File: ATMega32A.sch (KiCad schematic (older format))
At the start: 21 parts, among them J201 AVR-ISP-6, J202 UART, U201 ATmega32A-AU, Y201 16MHz

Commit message: Updating Atmega32A subboard
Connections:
- net labels added: A0, A1, A2, A3, A4, A5, A6, A7
- wire segments 56 -> 63

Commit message: Placing hierarchical labels on ATMega32A
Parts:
- added C?: 100n, Capacitor_SMD:C_0805_2012Metric_Pad1.15x1.40mm_HandSolder, symbol Device:C
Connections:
- net labels added: D1, D10_INT0, D11_INT1, D12_PWM, D13PWM, D14_PWM, D15_PWM, D16_SCL, D17_SDA, D18, D19, D2, D20, D21, D22, D23, D3, D4, D5, D6, D7, D8_Rx, D9_Tx, RST
- net labels removed: +12V, 1, 10_INT0, 11_INT1, 12_PWM, 13_PWM, 14_PWM, 15_PWM, 16_SCL, 17_SDA, 18, 19, 20, 21, 22, 23, 24_A0, 25_A1, 26_A2, 27_A3, 28_A4, 29_A5, 2_INT2, 30_A6, 31_A7, 3_PWM, 4_PWM
- wire segments 63 -> 93
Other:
- moved on the sheet: C?, R?

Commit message: Subboard done
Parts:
- removed C205, C207: 100n, Capacitor_SMD:C_1206_3216Metric_Pad1.42x1.75mm_HandSolder, symbol Device:C
- removed C206, C208: 100n, Capacitor_SMD:C_0805_2012Metric_Pad1.15x1.40mm_HandSolder, symbol Device:C
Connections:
- net D5 is gone; now on net 5_MOSI: U201.1 (PB5)
- net D6 is gone; now on net 6_MISO: U201.2 (PB6)
- net D7 is gone; now on net 7_SCK: U201.3 (PB7)
- net D13PWM renamed D13_PWM
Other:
- moved on the sheet: C?, R?

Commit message: Front LED
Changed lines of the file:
@@
 Text HLabel 2050 1150 0    97   Input ~ 0
 GND32
+Text HLabel 3000 1150 2    97   Input ~ 0
+GNDA32
 $EndSCHEMATC

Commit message: Cleanup MasterSCH
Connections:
- net D2 renamed D2_INT2
- net D3 renamed D3_OC0
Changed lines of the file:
@@
 D1
 Text HLabel 7000 3100 2    97   Input ~ 0
-D2
+D2_INT2
 Text HLabel 7000 3200 2    97   Input ~ 0
-D3
+D3_OC0
 Text HLabel 7000 3300 2    97   Input ~ 0
 D4

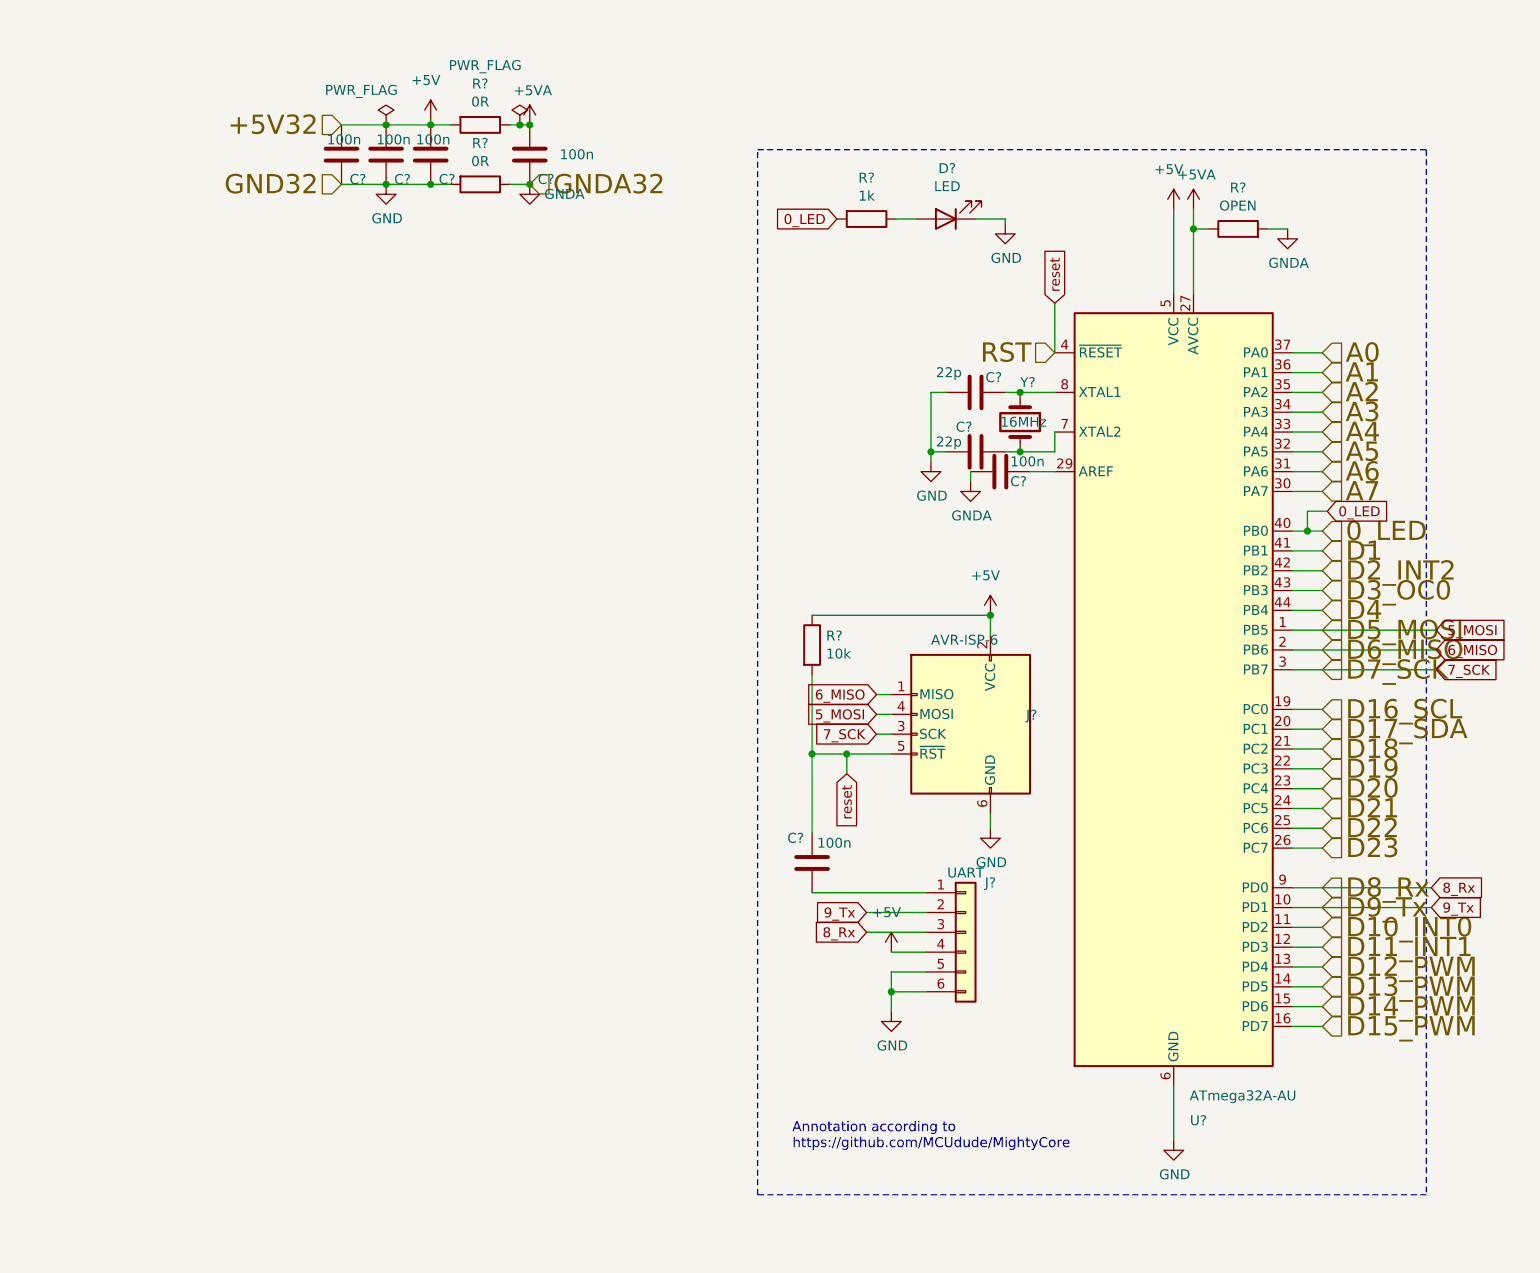
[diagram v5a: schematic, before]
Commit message: 5VA on Atmega32A
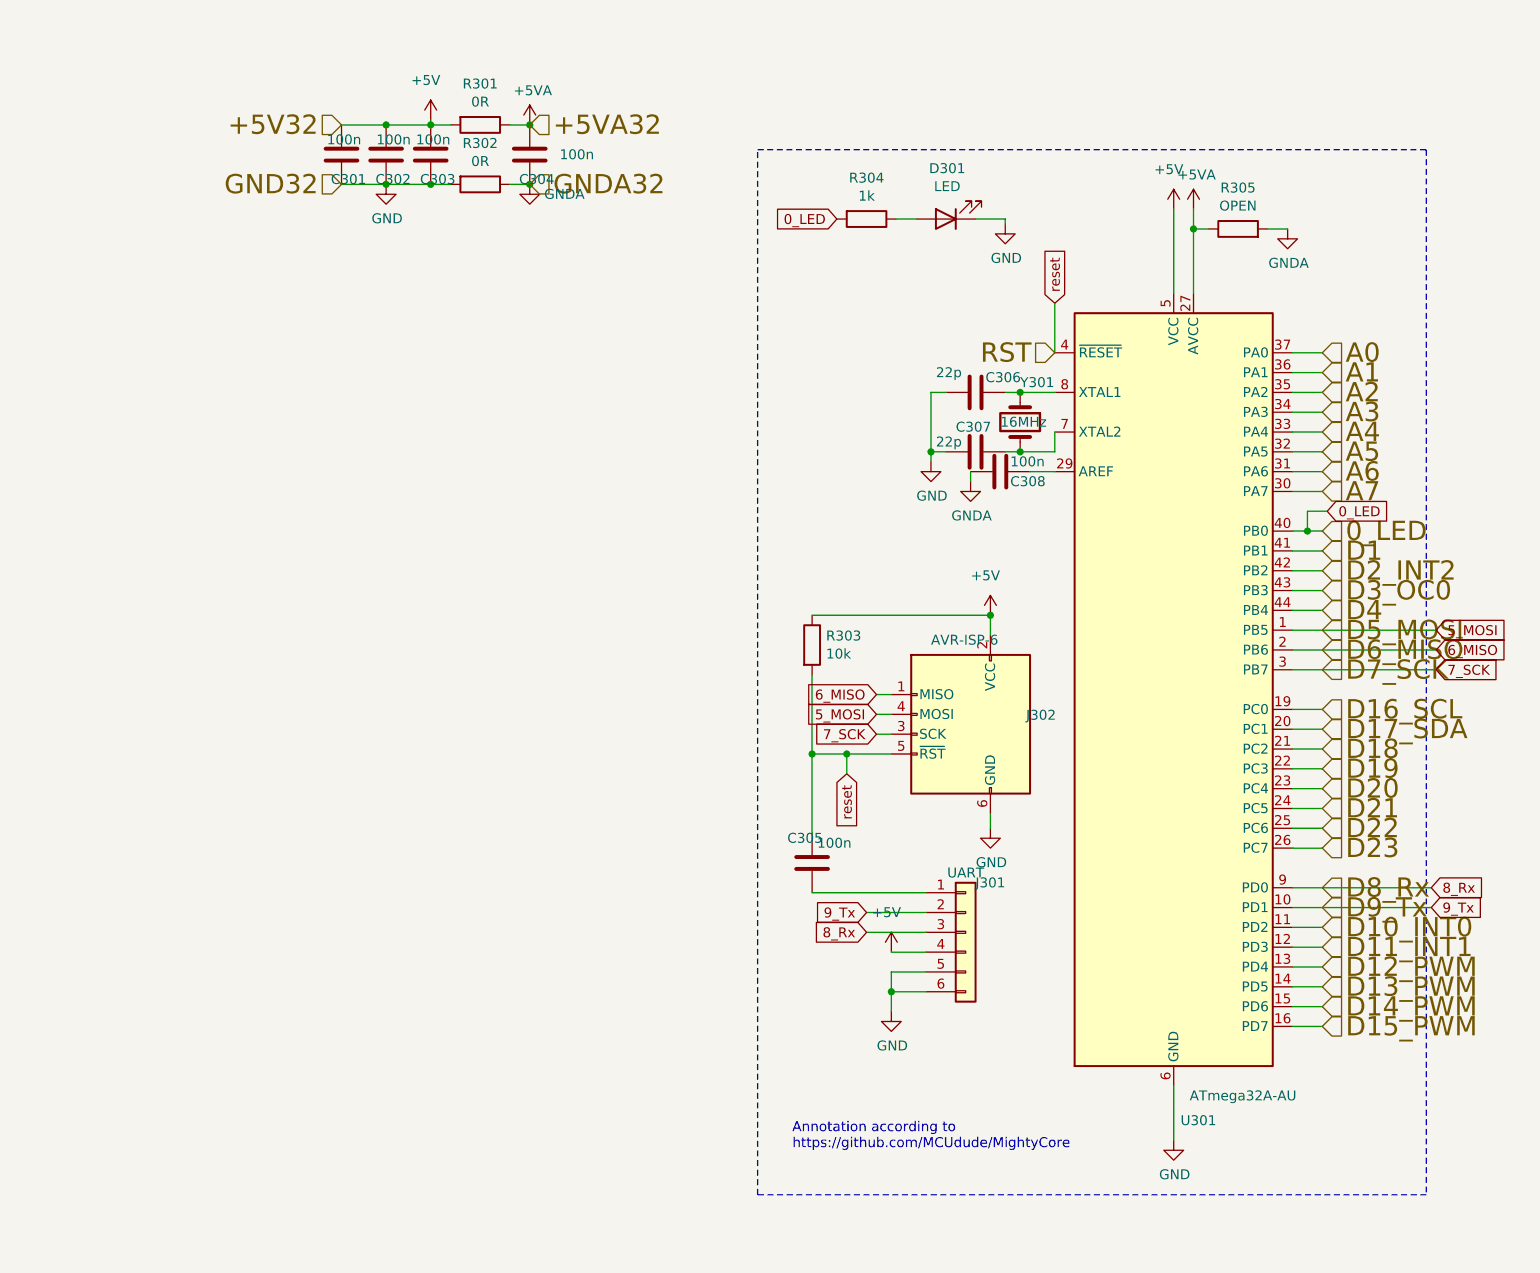
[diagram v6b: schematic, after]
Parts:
- gave numbers to parts that had none: 1

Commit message: Initial footprints and netlist
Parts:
- C201, C202, C203, C204, C209, C210, C211, C308: footprint Capacitor_SMD:C_0805_2012Metric_Pad1.15x1.40mm_HandSolder -> AJ:C_0805_AJ
- D201: footprint LED_SMD:LED_0805_2012Metric_Pad1.15x1.40mm_HandSolder -> AJ:D_0805_AJ
- R201, R202, R203, R205: footprint Resistor_SMD:R_0805_2012Metric_Pad1.15x1.40mm_HandSolder -> AJ:R_0805_AJ
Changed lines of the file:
@@
 F 0 "C305" H 4300 4700 50  0000 L CNN
 F 1 "100n" H 4450 4675 50  0000 L CNN
-F 2 "Capacitor_SMD:C_0805_2012Metric_Pad1.15x1.40mm_HandSolder" H 4463 4425 50  0001 C CNN
+F 2 "AJ:C_0805_AJ" H 4463 4425 50  0001 C CNN
 F 3 "~" H 4425 4575 50  0001 C CNN
 	1    4425 4575
@@
 F 0 "R303" H 4495 3521 50  0000 L CNN
 F 1 "10k" H 4495 3430 50  0000 L CNN
-F 2 "Resistor_SMD:R_0805_2012Metric_Pad1.15x1.40mm_HandSolder" V 4355 3475 50  0001 C CNN
+F 2 "AJ:R_0805_AJ" V 4355 3475 50  0001 C CNN
 F 3 "~" H 4425 3475 50  0001 C CNN
 	1    4425 3475
@@
 F 0 "C307" V 5125 2400 50  0000 L CNN
 F 1 "22p" V 5200 2300 50  0000 L CNN
-F 2 "Capacitor_SMD:C_0805_2012Metric_Pad1.15x1.40mm_HandSolder" H 5288 2350 50  0001 C CNN
+F 2 "AJ:C_0805_AJ" H 5288 2350 50  0001 C CNN
 F 3 "~" H 5250 2500 50  0001 C CNN
 	1    5250 2500
@@
 F 0 "C306" V 5175 2250 50  0000 L CNN
 F 1 "22p" V 5150 2000 50  0000 L CNN
-F 2 "Capacitor_SMD:C_0805_2012Metric_Pad1.15x1.40mm_HandSolder" H 5288 2050 50  0001 C CNN
+F 2 "AJ:C_0805_AJ" H 5288 2050 50  0001 C CNN
 F 3 "~" H 5250 2200 50  0001 C CNN
 	1    5250 2200
@@
 F 0 "R304" V 4493 1325 50  0000 C CNN
 F 1 "1k" V 4584 1325 50  0000 C CNN
-F 2 "Resistor_SMD:R_0805_2012Metric_Pad1.15x1.40mm_HandSolder" V 4630 1325 50  0001 C CNN
+F 2 "AJ:R_0805_AJ" V 4630 1325 50  0001 C CNN
 F 3 "~" H 4700 1325 50  0001 C CNN
 	1    4700 1325
@@
 F 0 "D301" H 5093 1070 50  0000 C CNN
 F 1 "LED" H 5093 1161 50  0000 C CNN
-F 2 "LED_SMD:LED_0805_2012Metric_Pad1.15x1.40mm_HandSolder" H 5100 1325 50  0001 C CNN
+F 2 "AJ:D_0805_AJ" H 5100 1325 50  0001 C CNN
 F 3 "~" H 5100 1325 50  0001 C CNN
 	1    5100 1325
@@
 F 0 "R305" V 6782 1375 50  0000 C CNN
 F 1 "OPEN" V 6691 1375 50  0000 C CNN
-F 2 "Resistor_SMD:R_0805_2012Metric_Pad1.15x1.40mm_HandSolder" V 6505 1375 50  0001 C CNN
+F 2 "AJ:R_0805_AJ" V 6505 1375 50  0001 C CNN
 F 3 "~" H 6575 1375 50  0001 C CNN
 	1    6575 1375
@@
 F 0 "R301" V 2543 850 50  0000 C CNN
 F 1 "0R" V 2634 850 50  0000 C CNN
-F 2 "Resistor_SMD:R_0805_2012Metric_Pad1.15x1.40mm_HandSolder" V 2680 850 50  0001 C CNN
+F 2 "AJ:R_0805_AJ" V 2680 850 50  0001 C CNN
 F 3 "~" H 2750 850 50  0001 C CNN
 	1    2750 850
@@
 F 0 "C304" H 2875 1125 50  0000 L CNN
 F 1 "100n" H 2675 1000 50  0000 L CNN
-F 2 "Capacitor_SMD:C_0805_2012Metric_Pad1.15x1.40mm_HandSolder" H 3038 850 50  0001 C CNN
+F 2 "AJ:C_0805_AJ" H 3038 850 50  0001 C CNN
 F 3 "~" H 3000 1000 50  0001 C CNN
 	1    3000 1000
@@
 F 0 "C303" H 2375 1125 50  0000 L CNN
 F 1 "100n" H 2400 925 50  0000 L CNN
-F 2 "Capacitor_SMD:C_0805_2012Metric_Pad1.15x1.40mm_HandSolder" H 2538 850 50  0001 C CNN
+F 2 "AJ:C_0805_AJ" H 2538 850 50  0001 C CNN
 F 3 "~" H 2500 1000 50  0001 C CNN
 	1    2500 1000
@@
 F 0 "C302" H 2150 1125 50  0000 L CNN
 F 1 "100n" H 2150 925 50  0000 L CNN
-F 2 "Capacitor_SMD:C_0805_2012Metric_Pad1.15x1.40mm_HandSolder" H 2313 850 50  0001 C CNN
+F 2 "AJ:C_0805_AJ" H 2313 850 50  0001 C CNN
 F 3 "~" H 2275 1000 50  0001 C CNN
 	1    2275 1000
@@
 F 0 "C301" H 1925 1125 50  0000 L CNN
 F 1 "100n" H 1950 925 50  0000 L CNN
-F 2 "Capacitor_SMD:C_0805_2012Metric_Pad1.15x1.40mm_HandSolder" H 2088 850 50  0001 C CNN
+F 2 "AJ:C_0805_AJ" H 2088 850 50  0001 C CNN
 F 3 "~" H 2050 1000 50  0001 C CNN
 	1    2050 1000
@@
 Wire Wire Line
 	6850 2900 6925 2900
-Wire Wire Line
-	6850 3000 7000 3000
-Wire Wire Line
-	7000 3100 6850 3100
-Wire Wire Line
-	6850 3200 7000 3200
-Wire Wire Line
-	7000 3300 6850 3300
 Wire Wire Line
 	6850 2700 7000 2700
@@
 F 0 "C308" V 5425 2650 50  0000 L CNN
 F 1 "100n" V 5325 2650 50  0000 L CNN
-F 2 "Capacitor_SMD:C_0805_2012Metric_Pad1.15x1.40mm_HandSolder" H 5413 2450 50  0001 C CNN
+F 2 "AJ:C_0805_AJ" H 5413 2450 50  0001 C CNN
 F 3 "~" H 5375 2600 50  0001 C CNN
 	1    5375 2600
@@
 Wire Wire Line
 	2900 850  3000 850
+Wire Wire Line
+	6850 3000 7000 3000
+Wire Wire Line
+	6850 3100 7000 3100
+Wire Wire Line
+	7000 3200 6850 3200
+Wire Wire Line
+	6850 3300 7000 3300
 $EndSCHEMATC

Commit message: Encoder 2
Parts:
- renumbered C201 to C301, C202 to C302, C203 to C303, C204 to C304, C211 to C305, C209 to C306, C210 to C307, D201 to D301, J202 to J301, J201 to J302, R201 to R301, R204 to R302, R205 to R303, R202 to R304, R203 to R305, U201 to U301, Y201 to Y301
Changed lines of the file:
@@
 P 6250 3700
 AR Path="/5CD50179" Ref="U?"  Part="1"
-AR Path="/5CD3F059/5CD50179" Ref="U201"  Part="1"
+AR Path="/5CD3F059/5CD50179" Ref="U?"  Part="1"
 AR Path="/608CA457/5CD3F059/5CD50179" Ref="U301"  Part="1"
 F 0 "U301" H 6375 1525 50  0000 C CNN
@@
 P 5225 3925
 AR Path="/5CD5017F" Ref="J?"  Part="1"
-AR Path="/5CD3F059/5CD5017F" Ref="J201"  Part="1"
+AR Path="/5CD3F059/5CD5017F" Ref="J?"  Part="1"
 AR Path="/608CA457/5CD3F059/5CD5017F" Ref="J302"  Part="1"
 F 0 "J302" H 4945 4021 50  0000 R CNN
@@
 P 5200 4925
 AR Path="/5CD50185" Ref="J?"  Part="1"
-AR Path="/5CD3F059/5CD50185" Ref="J202"  Part="1"
+AR Path="/5CD3F059/5CD50185" Ref="J?"  Part="1"
 AR Path="/608CA457/5CD3F059/5CD50185" Ref="J301"  Part="1"
 F 0 "J301" H 5325 5175 50  0000 C CNN
@@
 P 4425 4575
 AR Path="/5CD5019E" Ref="C?"  Part="1"
-AR Path="/5CD3F059/5CD5019E" Ref="C211"  Part="1"
+AR Path="/5CD3F059/5CD5019E" Ref="C?"  Part="1"
 AR Path="/608CA457/5CD3F059/5CD5019E" Ref="C305"  Part="1"
 F 0 "C305" H 4300 4700 50  0000 L CNN
@@
 P 4425 3475
 AR Path="/5CD501A6" Ref="R?"  Part="1"
-AR Path="/5CD3F059/5CD501A6" Ref="R205"  Part="1"
+AR Path="/5CD3F059/5CD501A6" Ref="R?"  Part="1"
 AR Path="/608CA457/5CD3F059/5CD501A6" Ref="R303"  Part="1"
 F 0 "R303" H 4495 3521 50  0000 L CNN
@@
 P 5475 2350
 AR Path="/5CD501CD" Ref="Y?"  Part="1"
-AR Path="/5CD3F059/5CD501CD" Ref="Y201"  Part="1"
+AR Path="/5CD3F059/5CD501CD" Ref="Y?"  Part="1"
 AR Path="/608CA457/5CD3F059/5CD501CD" Ref="Y301"  Part="1"
 F 0 "Y301" V 5275 2350 50  0000 L CNN
@@
 P 5250 2500
 AR Path="/5CD501D9" Ref="C?"  Part="1"
-AR Path="/5CD3F059/5CD501D9" Ref="C210"  Part="1"
+AR Path="/5CD3F059/5CD501D9" Ref="C?"  Part="1"
 AR Path="/608CA457/5CD3F059/5CD501D9" Ref="C307"  Part="1"
 F 0 "C307" V 5125 2400 50  0000 L CNN
@@
 P 5250 2200
 AR Path="/5CD501E0" Ref="C?"  Part="1"
-AR Path="/5CD3F059/5CD501E0" Ref="C209"  Part="1"
+AR Path="/5CD3F059/5CD501E0" Ref="C?"  Part="1"
 AR Path="/608CA457/5CD3F059/5CD501E0" Ref="C306"  Part="1"
 F 0 "C306" V 5175 2250 50  0000 L CNN
@@
 P 6825 1375
 AR Path="/5CD501E9" Ref="#PWR?"  Part="1"
-AR Path="/5CD3F059/5CD501E9" Ref="#PWR0206"  Part="1"
+AR Path="/5CD3F059/5CD501E9" Ref="#PWR?"  Part="1"
 AR Path="/608CA457/5CD3F059/5CD501E9" Ref="#PWR0315"  Part="1"
 F 0 "#PWR0315" H 6825 1125 50  0001 C CNN
@@
 P 5225 2650
 AR Path="/5CD501EF" Ref="#PWR?"  Part="1"
-AR Path="/5CD3F059/5CD501EF" Ref="#PWR0214"  Part="1"
+AR Path="/5CD3F059/5CD501EF" Ref="#PWR?"  Part="1"
 AR Path="/608CA457/5CD3F059/5CD501EF" Ref="#PWR0308"  Part="1"
 F 0 "#PWR0308" H 5225 2400 50  0001 C CNN
@@
 P 4700 1325
 AR Path="/5CD501F7" Ref="R?"  Part="1"
-AR Path="/5CD3F059/5CD501F7" Ref="R202"  Part="1"
+AR Path="/5CD3F059/5CD501F7" Ref="R?"  Part="1"
 AR Path="/608CA457/5CD3F059/5CD501F7" Ref="R304"  Part="1"
 F 0 "R304" V 4493 1325 50  0000 C CNN
@@
 P 5100 1325
 AR Path="/5CD501FD" Ref="D?"  Part="1"
-AR Path="/5CD3F059/5CD501FD" Ref="D201"  Part="1"
+AR Path="/5CD3F059/5CD501FD" Ref="D?"  Part="1"
 AR Path="/608CA457/5CD3F059/5CD501FD" Ref="D301"  Part="1"
 F 0 "D301" H 5093 1070 50  0000 C CNN
@@
 P 6575 1375
 AR Path="/5CD5023A" Ref="R?"  Part="1"
-AR Path="/5CD3F059/5CD5023A" Ref="R203"  Part="1"
+AR Path="/5CD3F059/5CD5023A" Ref="R?"  Part="1"
 AR Path="/608CA457/5CD3F059/5CD5023A" Ref="R305"  Part="1"
 F 0 "R305" V 6782 1375 50  0000 C CNN
@@
 P 6350 1275
 AR Path="/5CD5024D" Ref="#PWR?"  Part="1"
-AR Path="/5CD3F059/5CD5024D" Ref="#PWR0203"  Part="1"
+AR Path="/5CD3F059/5CD5024D" Ref="#PWR?"  Part="1"
 AR Path="/608CA457/5CD3F059/5CD5024D" Ref="#PWR0314"  Part="1"
 F 0 "#PWR0314" H 6350 1125 50  0001 C CNN
@@
 P 2750 850
 AR Path="/5CD5760D" Ref="R?"  Part="1"
-AR Path="/5CD3F059/5CD5760D" Ref="R201"  Part="1"
+AR Path="/5CD3F059/5CD5760D" Ref="R?"  Part="1"
 AR Path="/608CA457/5CD3F059/5CD5760D" Ref="R301"  Part="1"
 F 0 "R301" V 2543 850 50  0000 C CNN
@@
 P 3000 850
 AR Path="/5CD57617" Ref="#PWR?"  Part="1"
-AR Path="/5CD3F059/5CD57617" Ref="#PWR0204"  Part="1"
+AR Path="/5CD3F059/5CD57617" Ref="#PWR?"  Part="1"
 AR Path="/608CA457/5CD3F059/5CD57617" Ref="#PWR0303"  Part="1"
 F 0 "#PWR0303" H 3000 700 50  0001 C CNN
@@
 P 3000 1000
 AR Path="/5CD5761D" Ref="C?"  Part="1"
-AR Path="/5CD3F059/5CD5761D" Ref="C204"  Part="1"
+AR Path="/5CD3F059/5CD5761D" Ref="C?"  Part="1"
 AR Path="/608CA457/5CD3F059/5CD5761D" Ref="C304"  Part="1"
 F 0 "C304" H 2875 1125 50  0000 L CNN
@@
 P 2500 1000
 AR Path="/5CD57623" Ref="C?"  Part="1"
-AR Path="/5CD3F059/5CD57623" Ref="C203"  Part="1"
+AR Path="/5CD3F059/5CD57623" Ref="C?"  Part="1"
 AR Path="/608CA457/5CD3F059/5CD57623" Ref="C303"  Part="1"
 F 0 "C303" H 2375 1125 50  0000 L CNN
@@
 P 2275 1000
 AR Path="/5CD5762A" Ref="C?"  Part="1"
-AR Path="/5CD3F059/5CD5762A" Ref="C202"  Part="1"
+AR Path="/5CD3F059/5CD5762A" Ref="C?"  Part="1"
 AR Path="/608CA457/5CD3F059/5CD5762A" Ref="C302"  Part="1"
 F 0 "C302" H 2150 1125 50  0000 L CNN
@@
 P 2050 1000
 AR Path="/5CD57630" Ref="C?"  Part="1"
-AR Path="/5CD3F059/5CD57630" Ref="C201"  Part="1"
+AR Path="/5CD3F059/5CD57630" Ref="C?"  Part="1"
 AR Path="/608CA457/5CD3F059/5CD57630" Ref="C301"  Part="1"
 F 0 "C301" H 1925 1125 50  0000 L CNN
@@
 P 3000 1150
 AR Path="/5CD5763C" Ref="#PWR?"  Part="1"
-AR Path="/5CD3F059/5CD5763C" Ref="#PWR0208"  Part="1"
+AR Path="/5CD3F059/5CD5763C" Ref="#PWR?"  Part="1"
 AR Path="/608CA457/5CD3F059/5CD5763C" Ref="#PWR0304"  Part="1"
 F 0 "#PWR0304" H 3000 900 50  0001 C CNN
@@
 P 2750 1150
 AR Path="/5CD57648" Ref="R?"  Part="1"
-AR Path="/5CD3F059/5CD57648" Ref="R204"  Part="1"
+AR Path="/5CD3F059/5CD57648" Ref="R?"  Part="1"
 AR Path="/608CA457/5CD3F059/5CD57648" Ref="R302"  Part="1"
 F 0 "R302" V 2543 1150 50  0000 C CNN
